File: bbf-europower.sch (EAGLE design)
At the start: 13 parts, among them J1 CON_HEADER_2X05-PTH, J2 CON_HEADER_2X05-PTH

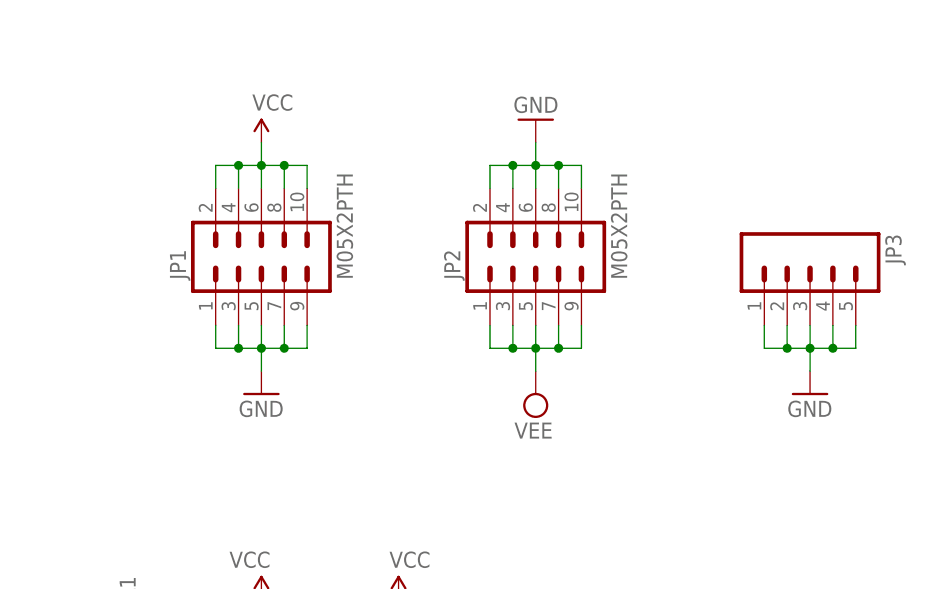
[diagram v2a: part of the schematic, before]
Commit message: the vcc with the farther away connector holes and wider board
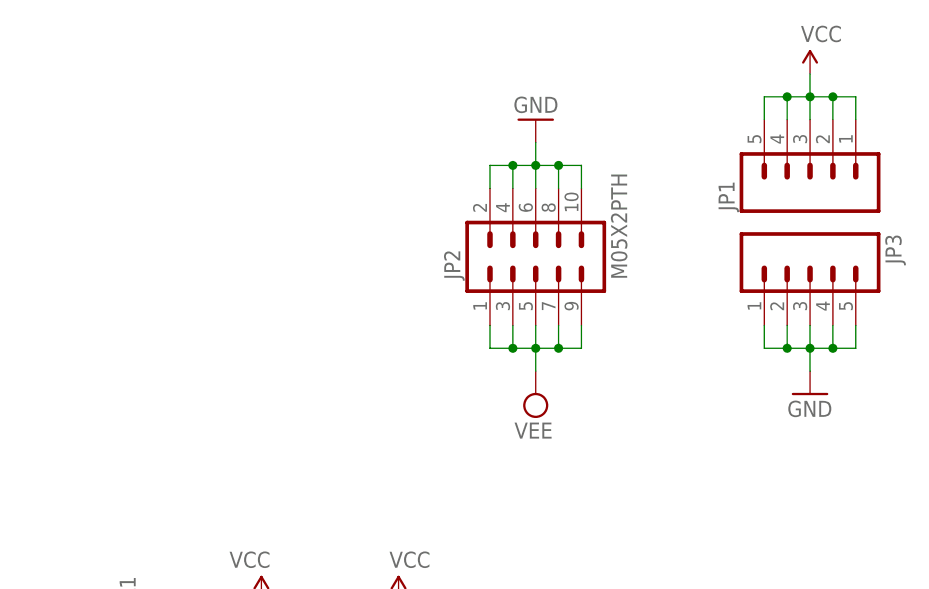
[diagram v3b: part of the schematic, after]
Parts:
- JP1: value M05X2PTH -> (none); device SparkFun:M05X2PTH -> SparkFun:M05PTH
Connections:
- net GND: no longer JP1.1, JP1.3, JP1.5, JP1.7, JP1.9
- net VCC: now also JP1.1, JP1.3, JP1.5; no longer JP1.10, JP1.6, JP1.8
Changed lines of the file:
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@@
 </classes>
 <parts>
-<part name="GND2" library="SparkFun" deviceset="GND" device=""/>
 <part name="GND4" library="SparkFun" deviceset="GND" device=""/>
 <part name="SUPPLY2" library="supply2" deviceset="VEE" device=""/>
-<part name="P+1" library="SparkFun" deviceset="VCC" device=""/>
-<part name="JP1" library="SparkFun" deviceset="M05X2" device="PTH"/>
 <part name="JP2" library="SparkFun" deviceset="M05X2" device="PTH"/>
 <part name="J1" library="tomatek" deviceset="CON_HEADER_2X05" device="-PTH" value="CON_HEADER_2X05-PTH"/>
@@
 <part name="JP3" library="SparkFun" deviceset="M05" device="PTH"/>
 <part name="GND5" library="SparkFun" deviceset="GND" device=""/>
+<part name="P+1" library="SparkFun" deviceset="VCC" device=""/>
+<part name="JP1" library="SparkFun" deviceset="M05" device="PTH"/>
 </parts>
 <sheets>
@@
 </plain>
 <instances>
-<instance part="GND2" gate="1" x="106.68" y="121.92" smashed="yes">
-<attribute name="VALUE" x="104.14" y="119.38" size="1.778" layer="96"/>
-</instance>
 <instance part="GND4" gate="1" x="137.16" y="152.4" smashed="yes" rot="R180">
 <attribute name="VALUE" x="139.7" y="154.94" size="1.778" layer="96" rot="R180"/>
@@
 <instance part="SUPPLY2" gate="G$1" x="137.16" y="121.92" smashed="yes" rot="R180">
 <attribute name="VALUE" x="139.065" y="118.745" size="1.778" layer="96" rot="R180"/>
-</instance>
-<instance part="P+1" gate="1" x="106.68" y="149.86" smashed="yes">
-<attribute name="VALUE" x="105.664" y="153.416" size="1.778" layer="96"/>
-</instance>
-<instance part="JP1" gate="G$1" x="106.68" y="137.16" smashed="yes" rot="R90">
-<attribute name="VALUE" x="116.84" y="134.62" size="1.778" layer="96" rot="R90"/>
-<attribute name="NAME" x="98.298" y="134.62" size="1.778" layer="95" rot="R90"/>
 </instance>
 <instance part="JP2" gate="G$1" x="137.16" y="137.16" smashed="yes" rot="R90">
@@
 <attribute name="VALUE" x="165.1" y="119.38" size="1.778" layer="96"/>
 </instance>
+<instance part="P+1" gate="1" x="167.64" y="157.48" smashed="yes">
+<attribute name="VALUE" x="166.624" y="161.036" size="1.778" layer="96"/>
+</instance>
+<instance part="JP1" gate="G$1" x="167.64" y="144.78" smashed="yes" rot="R90">
+<attribute name="VALUE" x="177.8" y="142.24" size="1.778" layer="96" rot="R90"/>
+<attribute name="NAME" x="159.258" y="142.24" size="1.778" layer="95" rot="R90"/>
+</instance>
 </instances>
 <busses>
@@
 <nets>
 <net name="GND" class="0">
-<segment>
-<wire x1="101.6" y1="129.54" x2="101.6" y2="127" width="0.1524" layer="91"/>
-<wire x1="101.6" y1="127" x2="104.14" y2="127" width="0.1524" layer="91"/>
-<wire x1="104.14" y1="127" x2="106.68" y2="127" width="0.1524" layer="91"/>
-<wire x1="106.68" y1="127" x2="109.22" y2="127" width="0.1524" layer="91"/>
-<wire x1="109.22" y1="127" x2="109.22" y2="129.54" width="0.1524" layer="91"/>
-<wire x1="106.68" y1="129.54" x2="106.68" y2="127" width="0.1524" layer="91"/>
-<wire x1="104.14" y1="129.54" x2="104.14" y2="127" width="0.1524" layer="91"/>
-<wire x1="106.68" y1="127" x2="106.68" y2="124.46" width="0.1524" layer="91"/>
-<wire x1="109.22" y1="127" x2="111.76" y2="127" width="0.1524" layer="91"/>
-<wire x1="111.76" y1="127" x2="111.76" y2="129.54" width="0.1524" layer="91"/>
-<junction x="106.68" y="127"/>
-<junction x="104.14" y="127"/>
-<junction x="109.22" y="127"/>
-<pinref part="GND2" gate="1" pin="GND"/>
-<pinref part="JP1" gate="G$1" pin="7"/>
-<pinref part="JP1" gate="G$1" pin="5"/>
-<pinref part="JP1" gate="G$1" pin="3"/>
-<pinref part="JP1" gate="G$1" pin="1"/>
-<pinref part="JP1" gate="G$1" pin="9"/>
-</segment>
 <segment>
 <wire x1="132.08" y1="144.78" x2="132.08" y2="147.32" width="0.1524" layer="91"/>
@@
 <net name="VCC" class="0">
 <segment>
-<wire x1="101.6" y1="144.78" x2="101.6" y2="147.32" width="0.1524" layer="91"/>
-<wire x1="101.6" y1="147.32" x2="104.14" y2="147.32" width="0.1524" layer="91"/>
-<wire x1="104.14" y1="147.32" x2="106.68" y2="147.32" width="0.1524" layer="91"/>
-<wire x1="106.68" y1="147.32" x2="109.22" y2="147.32" width="0.1524" layer="91"/>
-<wire x1="109.22" y1="147.32" x2="109.22" y2="144.78" width="0.1524" layer="91"/>
-<wire x1="106.68" y1="144.78" x2="106.68" y2="147.32" width="0.1524" layer="91"/>
-<wire x1="104.14" y1="144.78" x2="104.14" y2="147.32" width="0.1524" layer="91"/>
-<wire x1="106.68" y1="147.32" x2="106.68" y2="149.86" width="0.1524" layer="91"/>
-<wire x1="109.22" y1="147.32" x2="111.76" y2="147.32" width="0.1524" layer="91"/>
-<wire x1="111.76" y1="147.32" x2="111.76" y2="144.78" width="0.1524" layer="91"/>
-<junction x="104.14" y="147.32"/>
-<junction x="106.68" y="147.32"/>
-<junction x="109.22" y="147.32"/>
-<pinref part="P+1" gate="1" pin="VCC"/>
-<pinref part="JP1" gate="G$1" pin="8"/>
-<pinref part="JP1" gate="G$1" pin="6"/>
-<pinref part="JP1" gate="G$1" pin="4"/>
-<pinref part="JP1" gate="G$1" pin="2"/>
-<pinref part="JP1" gate="G$1" pin="10"/>
-</segment>
-<segment>
 <pinref part="P+3" gate="1" pin="VCC"/>
 <wire x1="121.92" y1="93.98" x2="121.92" y2="99.06" width="0.1524" layer="91"/>
@@
 <wire x1="106.68" y1="96.52" x2="106.68" y2="99.06" width="0.1524" layer="91"/>
 </segment>
+<segment>
+<pinref part="JP1" gate="G$1" pin="5"/>
+<wire x1="162.56" y1="152.4" x2="162.56" y2="154.94" width="0.1524" layer="91"/>
+<wire x1="162.56" y1="154.94" x2="165.1" y2="154.94" width="0.1524" layer="91"/>
+<pinref part="JP1" gate="G$1" pin="1"/>
+<wire x1="165.1" y1="154.94" x2="167.64" y2="154.94" width="0.1524" layer="91"/>
+<wire x1="167.64" y1="154.94" x2="170.18" y2="154.94" width="0.1524" layer="91"/>
+<wire x1="170.18" y1="154.94" x2="172.72" y2="154.94" width="0.1524" layer="91"/>
+<wire x1="172.72" y1="154.94" x2="172.72" y2="152.4" width="0.1524" layer="91"/>
+<pinref part="JP1" gate="G$1" pin="4"/>
+<wire x1="165.1" y1="152.4" x2="165.1" y2="154.94" width="0.1524" layer="91"/>
+<junction x="165.1" y="154.94"/>
+<pinref part="JP1" gate="G$1" pin="3"/>
+<wire x1="167.64" y1="152.4" x2="167.64" y2="154.94" width="0.1524" layer="91"/>
+<junction x="167.64" y="154.94"/>
+<pinref part="JP1" gate="G$1" pin="2"/>
+<wire x1="170.18" y1="152.4" x2="170.18" y2="154.94" width="0.1524" layer="91"/>
+<junction x="170.18" y="154.94"/>
+<pinref part="P+1" gate="1" pin="VCC"/>
+<wire x1="167.64" y1="154.94" x2="167.64" y2="157.48" width="0.1524" layer="91"/>
+</segment>
 </net>

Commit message: almost there
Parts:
- removed JP2: M05X2PTH, SparkFun:M05X2PTH
- added JP4, JP5: (no value), SparkFun:M05PTH
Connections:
- net GND: now also JP4.1, JP4.2, JP4.3, JP4.4, JP4.5; no longer JP2.10, JP2.2, JP2.4, JP2.6, JP2.8
- net VEE: now also JP5.1, JP5.2, JP5.3, JP5.4, JP5.5; no longer JP2.1, JP2.3, JP2.5, JP2.7, JP2.9
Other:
- moved on the sheet: JP1, JP3
